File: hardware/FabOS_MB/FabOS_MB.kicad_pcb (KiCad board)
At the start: 4 copper layers, 68 x 68 mm, 115 parts, among them J201 USB_A, J301 RJ45, J401 USB_C_Receptacle, J601 Conn_ST_STDC14, SW601 boot, SW602 SW_Push, SW603 SW_Push, SW604 SW_Push, SW605 SW_Push, U201 NCV7329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

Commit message: update paire diff
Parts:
- moved C308 0.96 mm to (132.5, 111.8)
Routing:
- net /ethernet/TD-: track 33.8 -> 37.9 mm
- net /ethernet/TD+: track 36.4 -> 33.8 mm
- net /ethernet/CT: track 3.94 -> 2.31 mm
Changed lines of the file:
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@@
 	(footprint "Capacitor_SMD:C_0402_1005Metric"
 		(layer "F.Cu")
-		(at 132.5 112.72 90)
+		(at 132.5 111.76 90)
 		(descr "Capacitor SMD 0402 (1005 Metric), square (rectangular) end terminal, IPC_7351 nominal, (Body size source: IPC-SM-782 page 76, https://www.pcb-3d.com/wordpress/wp-content/uploads/ipc-sm-782a_amendment_1_and_2.pdf), generated with kicad-footprint-generator")
 		(tags "capacitor")
@@
 		(tags "resistor")
 		(property "Reference" "R306"
-			(at 0 -1.17 360)
+			(at 0 -1.17 0)
 			(layer "F.SilkS")
 			(effects
@@
 		)
 		(property "Value" "10k"
-			(at 0 1.17 360)
+			(at 0 1.17 0)
 			(layer "F.Fab")
 			(effects
@@
 		)
 		(fp_text user "${REFERENCE}"
-			(at 0 0 360)
+			(at 0 0 0)
 			(layer "F.Fab")
 			(effects
@@
 	)
 	(segment
-		(start 133.08 113.78)
-		(end 132.5 113.2)
-		(width 0.15)
-		(layer "F.Cu")
-		(net 8)
-	)
-	(segment
-		(start 133.8925 113.78)
-		(end 133.08 113.78)
-		(width 0.15)
-		(layer "F.Cu")
-		(net 8)
-	)
-	(segment
 		(start 134.2 118.12)
 		(end 133.2 118.12)
@@
 	)
 	(segment
-		(start 132.516494 120.6016)
-		(end 131.691494 119.7766)
+		(start 133.187849 114.7316)
+		(end 133.236249 114.78)
 		(width 0.2)
 		(layer "F.Cu")
@@
 	)
 	(segment
-		(start 131.2984 113.783506)
-		(end 131.2984 111.116494)
+		(start 124.6616 111.462506)
+		(end 125.305506 110.8186)
 		(width 0.2)
 		(layer "F.Cu")
@@
 	)
 	(segment
-		(start 133.187849 114.7316)
-		(end 132.246494 114.7316)
+		(start 129.7194 123.487494)
+		(end 129.075494 124.1314)
 		(width 0.2)
 		(layer "F.Cu")
@@
 	)
 	(segment
-		(start 133.8925 114.78)
-		(end 133.236249 114.78)
+		(start 125.305506 110.8186)
+		(end 128.694494 110.8186)
 		(width 0.2)
 		(layer "F.Cu")
@@
 	)
 	(segment
-		(start 129.5184 119.7766)
-		(end 128.45 120.845)
+		(start 127.7 120.845)
+		(end 129.669789 120.845)
 		(width 0.2)
 		(layer "F.Cu")
@@
 	)
 	(segment
-		(start 140.1016 112.616494)
-		(end 140.1016 119.183506)
+		(start 128.694494 110.8186)
+		(end 132.607494 114.7316)
 		(width 0.2)
 		(layer "F.Cu")
@@
 	)
 	(segment
-		(start 131.691494 119.7766)
-		(end 129.5184 119.7766)
+		(start 129.075494 124.1314)
+		(end 125.813506 124.1314)
 		(width 0.2)
 		(layer "F.Cu")
@@
 	)
 	(segment
-		(start 140.1016 119.183506)
-		(end 138.683506 120.6016)
+		(start 124.6616 122.979494)
+		(end 124.6616 111.462506)
 		(width 0.2)
 		(layer "F.Cu")
@@
 	)
 	(segment
-		(start 132.246494 114.7316)
-		(end 131.2984 113.783506)
+		(start 133.236249 114.78)
+		(end 133.8925 114.78)
 		(width 0.2)
 		(layer "F.Cu")
@@
 	)
 	(segment
-		(start 133.236249 114.78)
-		(end 133.187849 114.7316)
+		(start 129.669789 120.845)
+		(end 129.7194 120.894611)
 		(width 0.2)
 		(layer "F.Cu")
@@
 	)
 	(segment
-		(start 132.516494 109.8984)
-		(end 137.383506 109.8984)
+		(start 125.813506 124.1314)
+		(end 124.6616 122.979494)
 		(width 0.2)
 		(layer "F.Cu")
@@
 	)
 	(segment
-		(start 131.2984 111.116494)
-		(end 132.516494 109.8984)
+		(start 132.607494 114.7316)
+		(end 133.187849 114.7316)
 		(width 0.2)
 		(layer "F.Cu")
@@
 	)
 	(segment
-		(start 138.683506 120.6016)
-		(end 132.516494 120.6016)
+		(start 129.7194 120.894611)
+		(end 129.7194 123.487494)
 		(width 0.2)
 		(layer "F.Cu")
@@
 	)
 	(segment
-		(start 137.383506 109.8984)
-		(end 140.1016 112.616494)
+		(start 124.2584 111.295494)
+		(end 125.138494 110.4154)
 		(width 0.2)
 		(layer "F.Cu")
-		(net 68)
+		(net 70)
 	)
 	(segment
-		(start 133.8925 114.28)
-		(end 133.236249 114.28)
+		(start 132.774506 114.3284)
+		(end 133.187849 114.3284)
 		(width 0.2)
 		(layer "F.Cu")
@@
 	)
 	(segment
-		(start 131.7016 111.283506)
-		(end 132.683506 110.3016)
+		(start 133.236249 114.28)
+		(end 133.8925 114.28)
 		(width 0.2)
 		(layer "F.Cu")
@@
 	)
 	(segment
-		(start 133.187849 114.3284)
-		(end 132.413506 114.3284)
+		(start 127.7 118.305)
+		(end 128.295 118.9)
 		(width 0.2)
 		(layer "F.Cu")
@@
 	)
 	(segment
-		(start 132.683506 110.3016)
-		(end 137.216494 110.3016)
+		(start 129.242506 124.5346)
+		(end 125.646494 124.5346)
 		(width 0.2)
 		(layer "F.Cu")
@@
 	)
 	(segment
-		(start 128.45 118.305)
-		(end 127.7 118.305)
+		(start 125.646494 124.5346)
+		(end 124.2584 123.146506)
 		(width 0.2)
 		(layer "F.Cu")
@@
 	)
 	(segment
-		(start 132.413506 114.3284)
-		(end 131.7016 113.616494)
+		(start 128.45 118.305)
+		(end 127.7 118.305)
 		(width 0.2)
 		(layer "F.Cu")
@@
 	)
 	(segment
-		(start 139.6984 112.783506)
-		(end 139.6984 119.016494)
+		(start 130.1226 123.654506)
+		(end 129.242506 124.5346)
 		(width 0.2)
 		(layer "F.Cu")
@@
 	)
 	(segment
-		(start 139.6984 119.016494)
-		(end 138.516494 120.1984)
+		(start 125.138494 110.4154)
+		(end 128.861506 110.4154)
 		(width 0.2)
 		(layer "F.Cu")
@@
 	)
 	(segment
-		(start 129.5184 119.3734)
-		(end 128.45 118.305)
+		(start 129.125 119.73)
+		(end 130.1226 120.7276)
 		(width 0.2)
 		(layer "F.Cu")
@@
 	)
 	(segment
-		(start 132.683506 120.1984)
-		(end 131.858506 119.3734)
+		(start 129.125 118.9)
+		(end 129.125 119.73)
 		(width 0.2)
 		(layer "F.Cu")
@@
 	)
 	(segment
-		(start 133.236249 114.28)
-		(end 133.187849 114.3284)
+		(start 124.2584 123.146506)
+		(end 124.2584 111.295494)
 		(width 0.2)
 		(layer "F.Cu")
@@
 	)
 	(segment
-		(start 138.516494 120.1984)
-		(end 132.683506 120.1984)
+		(start 128.861506 110.4154)
+		(end 132.774506 114.3284)
 		(width 0.2)
 		(layer "F.Cu")
@@
 	)
 	(segment
-		(start 131.7016 113.616494)
-		(end 131.7016 111.283506)
+		(start 130.1226 120.7276)
+		(end 130.1226 123.654506)
 		(width 0.2)
 		(layer "F.Cu")
@@
 	)
 	(segment
-		(start 131.858506 119.3734)
-		(end 129.5184 119.3734)
+		(start 128.295 118.9)
+		(end 129.125 118.9)
 		(width 0.2)
 		(layer "F.Cu")
@@
 	)
 	(segment
-		(start 137.216494 110.3016)
-		(end 139.6984 112.783506)
+		(start 133.187849 114.3284)
+		(end 133.236249 114.28)
 		(width 0.2)
 		(layer "F.Cu")

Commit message: Update pcb
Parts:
- moved Y301 28.3 mm to (134.9, 122.7), turned to 180 degrees
- moved R306 22.6 mm to (141.6, 133.5)
- moved R305 20.8 mm to (141.6, 130.5), turned to 180 degrees
- moved R302 9.70 mm to (139.4, 116.8), turned to 180 degrees
- moved R304 7.85 mm to (141.8, 123.8)
- moved R318 3.51 mm to (141.7, 122.8)
- moved R307 3.35 mm to (141.8, 125.7)
- moved R310 3.19 mm to (141.6, 131.5), turned to 180 degrees
- moved R309 3.18 mm to (141.6, 128.6)
- moved R312 2.39 mm to (141.6, 132.5)
- moved R308 2.22 mm to (139.9, 118.6), turned to -90 degrees
- moved R301 1.87 mm to (141.8, 126.7)
- moved R303 1.05 mm to (141.6, 129.6), turned to 180 degrees
- moved C308 0.90 mm to (132.7, 112.6)
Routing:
- net /ETH_TXD1: track 0.89 -> 25.8 mm, vias 1 -> 2
- net /ETH_REF_CLK: track 1.54 -> 25.5 mm, vias 1 -> 2
- net /ETH_TXD0: track 1.11 -> 24.6 mm, vias 1 -> 2
- net /ETH_TX_EN: track 1.50 -> 23.1 mm, vias 1 -> 2
- net Net-(U301-~{INT}/REFCLKO): track 2.65 -> 23.6 mm, vias 0 -> 2
- net /ethernet/CT: track 2.31 -> 22.5 mm, vias 0 -> 2
- net /ETH_MDI0: track 0.00 -> 20.1 mm, vias 0 -> 4
- net Net-(U301-CRS_DV/MODE2): track 0.00 -> 19.4 mm, vias 0 -> 2
- net /ETH_MDC: track 1.31 -> 16.5 mm, vias 1 -> 2
- net /NRST_ETH: track 0.94 -> 10.4 mm, vias 1 -> 0
- net GND: track 11.3 -> 16.4 mm, vias 3 -> 4
- net Net-(U301-RXD1/MODE1): track 0.34 -> 4.80 mm
- net /ethernet/TD+: track 33.8 -> 35.8 mm
- net /ethernet/VDDCR: track 3.01 -> 2.20 mm, vias 1 -> 0
- net /ethernet/TD-: track 37.9 -> 38.5 mm

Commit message: routage
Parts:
- added C306: 100n, Capacitor_SMD:C_0402_1005Metric, F.Cu at (140.7, 96.6)
- moved R320 59.8 mm to (113.5, 110.1)
- moved R321 54.2 mm to (114.0, 121.5), turned to 0 degrees
- moved R322 40.3 mm to (114.0, 122.7), turned to 0 degrees
- moved C311 35.8 mm to (129.2, 104.7)
- moved R318 26.5 mm to (144.8, 149.1), turned to -90 degrees
- moved C617 25.9 mm to (149.1, 104.6), turned to 90 degrees
- moved C602 21.7 mm to (142.0, 120.9)
- moved C611 19.8 mm to (141.8, 104.4)
- moved R312 18.7 mm to (132.1, 116.5), turned to 180 degrees
- moved C303 16.4 mm to (138.0, 122.0), turned to 90 degrees
- moved C305 15.6 mm to (132.7, 122.3), turned to -90 degrees
- moved R317 15.3 mm to (146.8, 149.1), turned to -90 degrees
- moved C613 12.5 mm to (146.3, 97.9)
- moved C614 12.5 mm to (146.3, 99.1)
- moved R316 12.4 mm to (147.8, 149.1), turned to -90 degrees
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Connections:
- C311 pad 2: Earth -> GND
- U303 pad 2: Earth -> GND
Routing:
- net /ETH_TXD1: track 25.8 -> 0.03 mm, vias 2 -> 0
- net /ETH_TXD0: track 24.6 -> 0.29 mm, vias 2 -> 0
- net /ETH_TX_EN: track 23.1 -> 0.04 mm, vias 2 -> 0
- net /ethernet/CT: track 22.5 -> 38.4 mm
- net GND: track 16.4 -> 26.6 mm, vias 4 -> 6
- net Net-(U301-XTAL2): track 0.00 -> 8.69 mm
- net Net-(U301-XTAL1/CLKIN): track 0.00 -> 6.14 mm
- net /ethernet/RD+: track 7.61 -> 9.38 mm
- net /ethernet/RD-: track 7.61 -> 9.38 mm
- net /ethernet/LED1+: track 0.00 -> 1.67 mm, vias 0 -> 1
- net /ethernet/TD+: track 35.8 -> 37.3 mm
- net /ethernet/TD-: track 38.5 -> 40.0 mm
- net /ethernet/LED2+: track 0.00 -> 1.12 mm, vias 0 -> 1
- net Net-(J301-Pad7): track 0.00 -> 1.02 mm
- net Net-(J301-Pad4): track 0.00 -> 1.02 mm

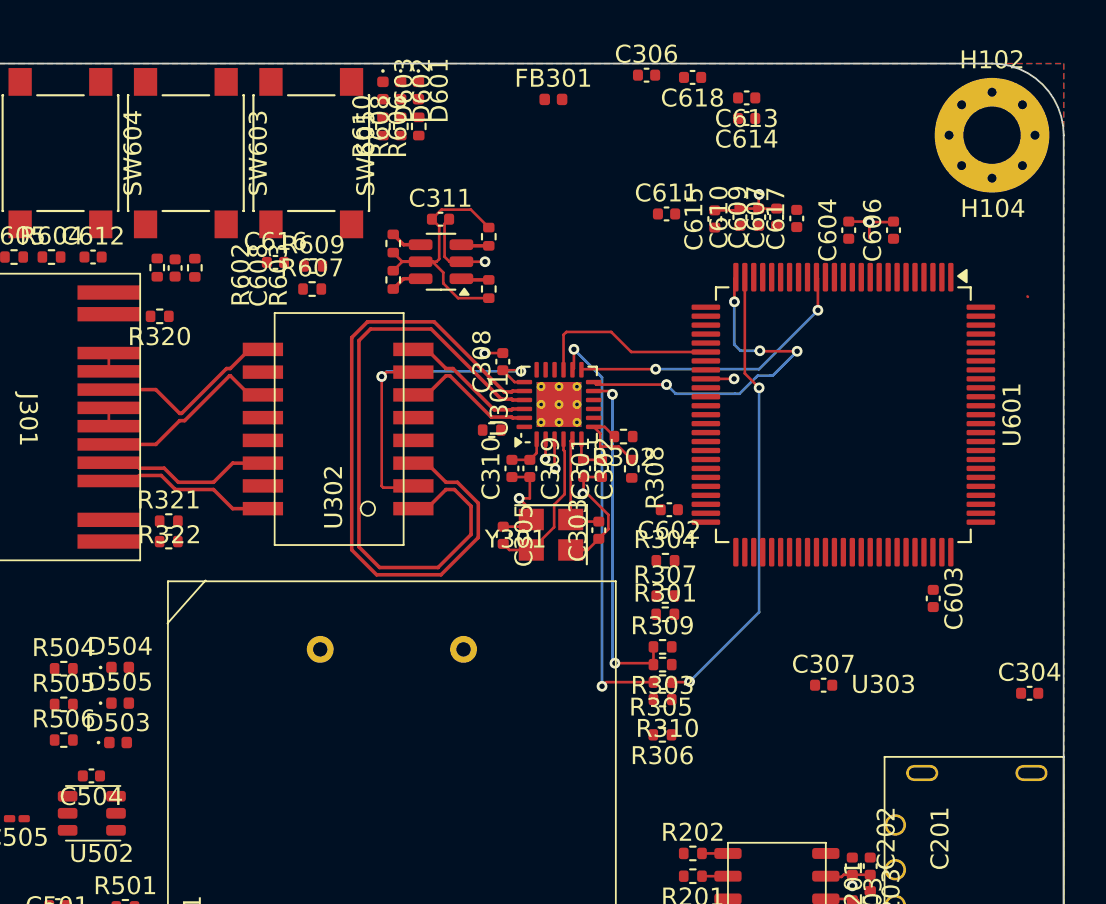
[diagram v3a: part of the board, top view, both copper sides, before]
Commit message: Update PCB
Plus que 100 à router
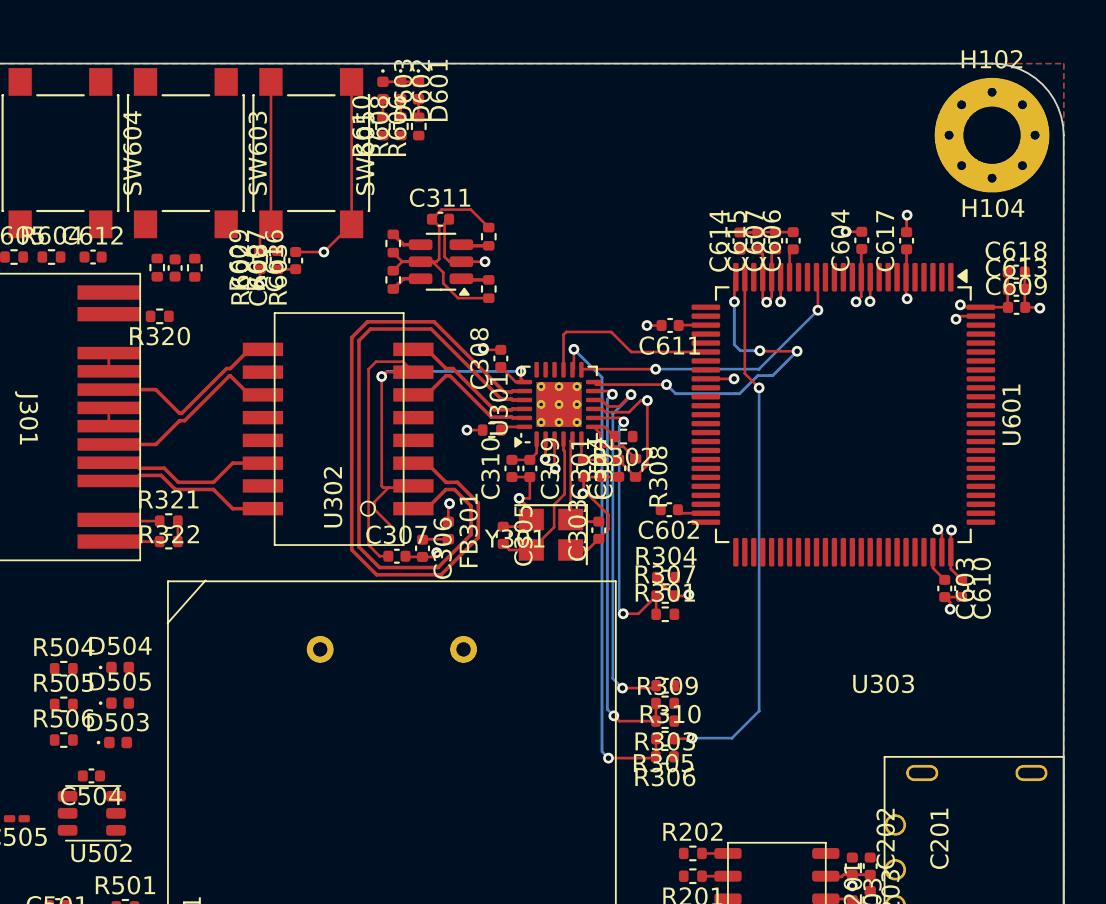
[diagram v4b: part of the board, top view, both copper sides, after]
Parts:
- moved C306 29.2 mm to (128.2, 123.1), turned to -90 degrees
- moved C304 26.2 mm to (139.2, 118.6), turned to 90 degrees
- moved C307 24.9 mm to (126.8, 123.5)
- moved FB301 24.8 mm to (129.7, 122.1), turned to -90 degrees
- moved C610 24.1 mm to (158.3, 125.3), turned to -90 degrees
- moved C618 21.1 mm to (161.3, 107.6), turned to 0 degrees
- moved C613 18.5 mm to (161.4, 108.6), turned to 0 degrees
- moved C609 15.3 mm to (161.4, 109.6), turned to 0 degrees
- moved C614 6.85 mm to (145.9, 105.9), turned to 90 degrees
- moved C617 6.26 mm to (155.2, 105.9)
- moved C611 6.23 mm to (142.0, 110.6), turned to 180 degrees
- moved C606 5.63 mm to (148.9, 105.9)
- moved R303 3.16 mm to (141.8, 132.7)
- moved R305 3.16 mm to (141.8, 133.7)
- moved R309 3.16 mm to (141.8, 131.7)
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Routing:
- net +3.3V: track 0.00 -> 38.5 mm, vias 0 -> 9
- net GND: track 26.6 -> 53.1 mm, vias 6 -> 16
- net Net-(U301-RXER/PHYAD0): track 0.00 -> 22.0 mm, vias 0 -> 2
- net /ethernet/CT: track 38.4 -> 57.1 mm
- net Net-(U301-RXD0/MODE0): track 0.00 -> 15.9 mm, vias 0 -> 2
- net Net-(R607-Pad2): track 0.00 -> 10.7 mm
- net Net-(U301-~{INT}/REFCLKO): track 23.6 -> 28.5 mm
- net /ETH_REF_CLK: track 25.5 -> 29.9 mm
- net Net-(U301-CRS_DV/MODE2): track 19.4 -> 22.8 mm
- net /ethernet/LED2+: track 1.12 -> 3.99 mm
- net Net-(J301-LED2-): track 0.00 -> 2.83 mm
- net Net-(U601-VCAP_2): track 0.00 -> 1.87 mm
- net Net-(U601-VCAP_1): track 0.00 -> 1.64 mm
- net Net-(U301-RBIAS): track 0.00 -> 1.38 mm
- net Net-(D601-A): track 0.00 -> 1.02 mm
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
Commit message: update pcb
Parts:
- moved C617 20.8 mm to (141.9, 121.8), turned to 180 degrees
- moved C612 6.84 mm to (103.0, 106.7)
- moved R604 4.66 mm to (103.0, 105.7)
- moved D504 4.24 mm to (111.3, 133.9), turned to 180 degrees
- moved D503 4.11 mm to (111.5, 129.8), turned to 180 degrees
- moved R605 3.24 mm to (103.0, 104.7)
- moved R505 2.18 mm to (108.2, 133.9)
- moved R603 2.10 mm to (113.4, 107.4), turned to 90 degrees
- moved R506 2.06 mm to (108.2, 131.7)
- moved R602 1.00 mm to (114.4, 107.4), turned to 90 degrees
- moved C608 1.00 mm to (115.4, 107.4), turned to 90 degrees
- moved R501 0.68 mm to (111.7, 143.8)
- turned D505 to 180 degrees
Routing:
- net GND: track 53.1 -> 82.1 mm, vias 16 -> 20
- net /ETH_TXD1: track 0.03 -> 24.3 mm, vias 0 -> 2
- net /ETH_CRS_DV: track 0.00 -> 23.8 mm, vias 0 -> 2
- net /ETH_TXD0: track 0.29 -> 22.2 mm, vias 0 -> 2
- net /ETH_TX_EN: track 0.04 -> 21.7 mm, vias 0 -> 2
- net /ETH_RXD0: track 0.00 -> 17.2 mm, vias 0 -> 2
- net Net-(R604-Pad2): track 0.00 -> 11.3 mm
- net Net-(R602-Pad2): track 0.00 -> 11.1 mm
- net Net-(U502-SW): track 0.00 -> 3.13 mm
- net Net-(D503-A): track 0.00 -> 2.28 mm
- net Net-(D504-A): track 0.00 -> 2.22 mm
- net Net-(D505-A): track 0.00 -> 2.15 mm
- net /ETH_RXD1: track 1.57 -> 0.00 mm, vias 1 -> 0
- net Net-(U502-VBST): track 0.00 -> 1.51 mm
- net /STM32/BTN2: track 0.00 -> 1.01 mm
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
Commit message: update pcb
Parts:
- moved R503 13.7 mm to (111.4, 133.3)
- moved R502 12.7 mm to (111.4, 132.3)
- moved R501 11.0 mm to (109.9, 132.8), turned to 90 degrees
- moved C503 7.44 mm to (111.5, 138.8), turned to 0 degrees
- moved C501 5.64 mm to (111.5, 139.9), turned to 180 degrees
- moved C506 4.94 mm to (103.9, 138.0), turned to 90 degrees
- moved L501 4.36 mm to (105.9, 140.2), turned to 0 degrees
- moved C502 4.11 mm to (111.5, 141.1), turned to 0 degrees
- moved D503 3.77 mm to (111.8, 126.0)
- moved D504 3.77 mm to (111.7, 130.2)
- moved R504 3.77 mm to (108.6, 126.0)
- moved R505 3.77 mm to (108.6, 130.2)
- moved D505 3.77 mm to (111.7, 128.0)
- moved R506 3.77 mm to (108.6, 128.0)
- moved C504 1.92 mm to (107.8, 136.1), turned to -90 degrees
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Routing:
- net /5V_Flyback: track 4.05 -> 66.8 mm, vias 1 -> 3
- net /power/5V_max: track 0.00 -> 25.2 mm
- net /5V_USB: track 0.00 -> 18.8 mm
- net GND: track 82.1 -> 97.6 mm, vias 20 -> 30
- net +3.3V: track 38.0 -> 45.4 mm, vias 10 -> 13
- net Net-(U502-SW): track 3.13 -> 7.85 mm
- net Net-(U601-BOOT0): track 0.00 -> 3.13 mm
- net Net-(U502-VFB): track 0.00 -> 2.37 mm
- net Net-(U502-EN): track 0.00 -> 1.34 mm
